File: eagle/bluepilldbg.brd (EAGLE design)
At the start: 39.4 x 19 mm, 9 parts

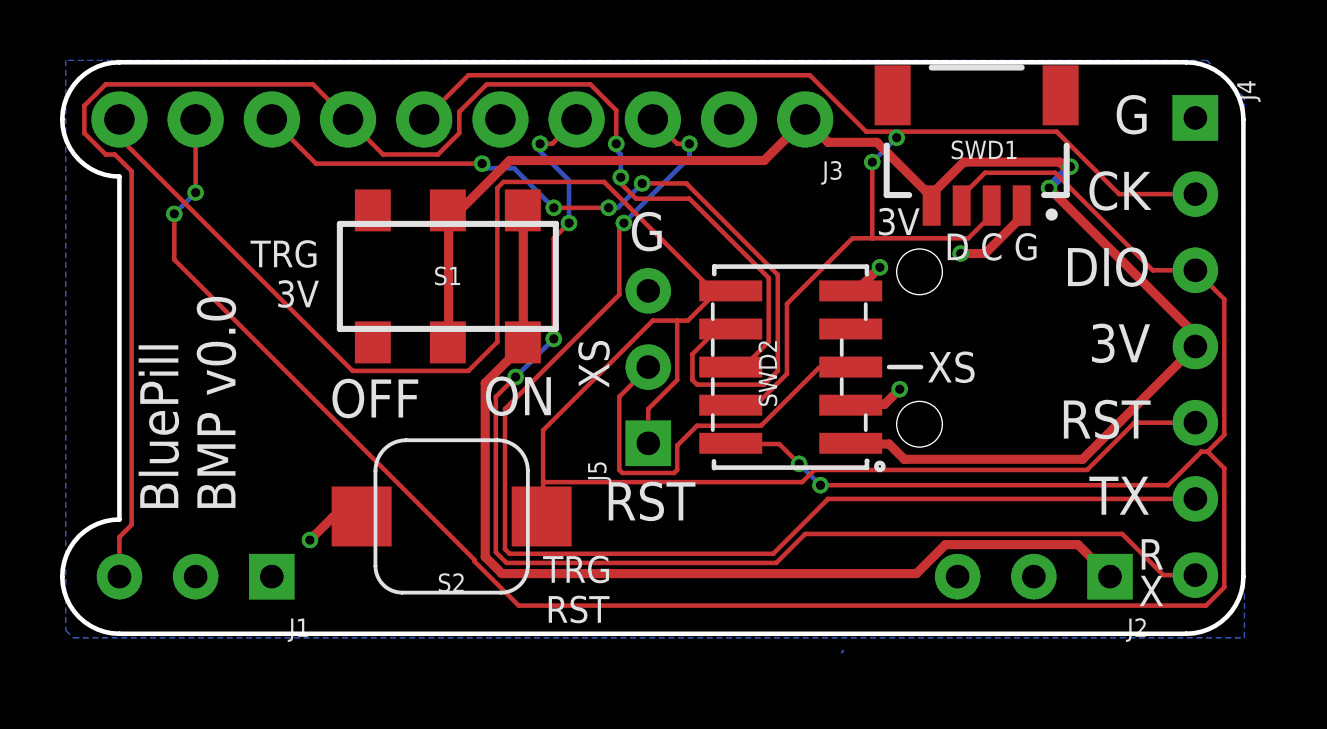
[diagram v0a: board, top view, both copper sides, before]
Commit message: smaller pcb
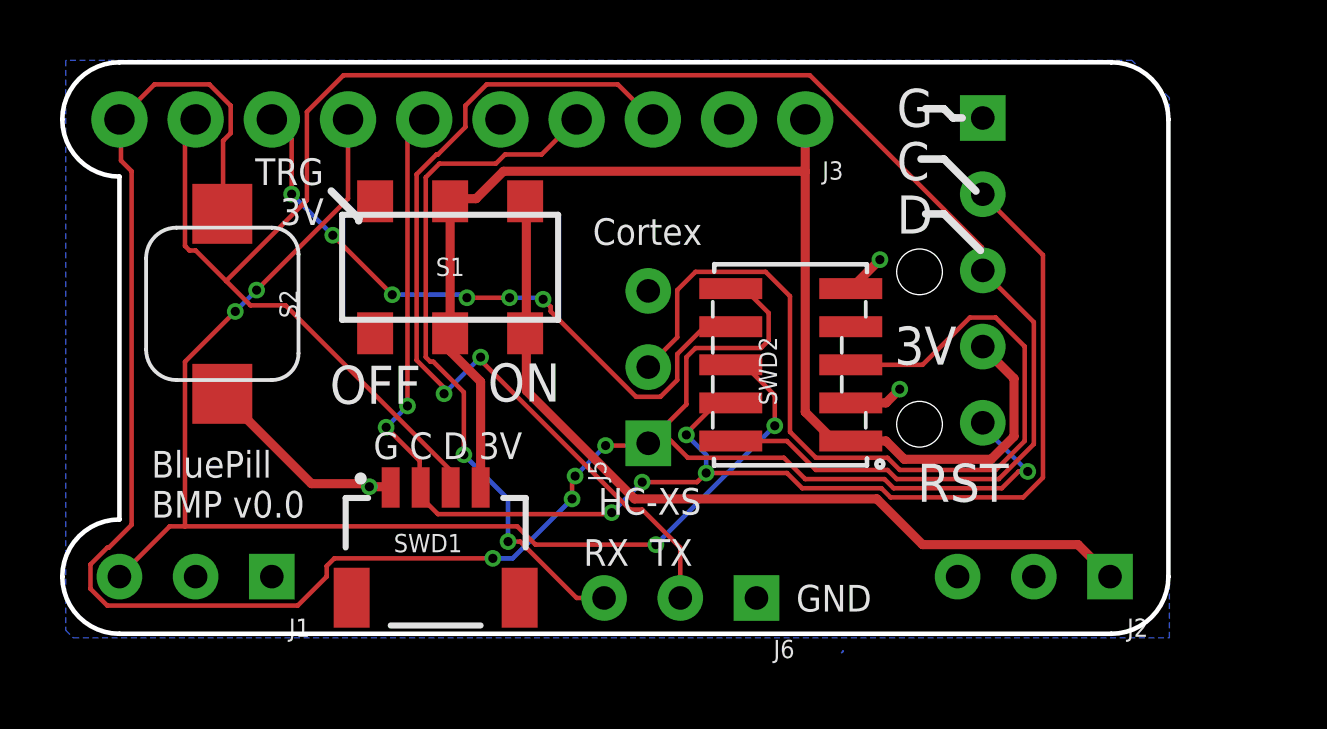
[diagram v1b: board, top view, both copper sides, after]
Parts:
- added J6: (no value), pcnt:1X03_NO_SILK
- J4: device SparkFun-Connectors:1X07_NO_SILK -> pcnt:1X05_SMALLHOLE
- moved SWD1 20.3 mm to (13.1, 5.51), turned to 0 degrees
- moved S2 10.4 mm to (5.97, 11.6), turned to 270 degrees
- moved J4 7.09 mm to (31.3, 17.8)
- moved S1 0.31 mm to (13.6, 12.9)
- moved SWD2 0.08 mm to (24.9, 9.60)
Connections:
- net GND: now also J6.1
- net RX: now also J6.3; no longer J4.7
- net TX: now also J6.2; no longer J4.6
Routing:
- net RX: track 41.0 -> 23.1 mm, vias 4 -> 2
- net HACK_RST: track 13.5 -> 30.6 mm
- net SWDIO: track 83.2 -> 67.4 mm, vias 4 -> 0
- net TX: track 41.4 -> 30.5 mm
- net VREF: track 50.3 -> 43.3 mm, vias 2 -> 0
- net TDO: track 49.9 -> 43.2 mm, vias 2 -> 4
- net TDI: track 28.5 -> 21.8 mm, vias 4 -> 6
- net VCC: track 34.0 -> 28.4 mm
- net SWCLK: track 44.8 -> 49.5 mm, vias 2 -> 6
- net GND: track 8.13 -> 10.1 mm, vias 4 -> 3
- net RST: track 69.5 -> 71.2 mm, vias 0 -> 5
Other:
- board size 39.4 x 19 mm -> 36.9 x 19 mm
- board text added: "Cortex"
- board text added: "G C D"
- board text added: "G C D 3V"
- board text added: "GND"
- board text added: "GND TX RX"
- board text added: "HC-XS"
- board text added: "RX TX"
- board text removed: "D C G"
- board text removed: "G"
- board text removed: "G CK DIO 3V RST TX"
- board text removed: "R X"
- board text removed: "TRG RST"
- board text removed: "XS"

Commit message: Nicer schematics; place part names
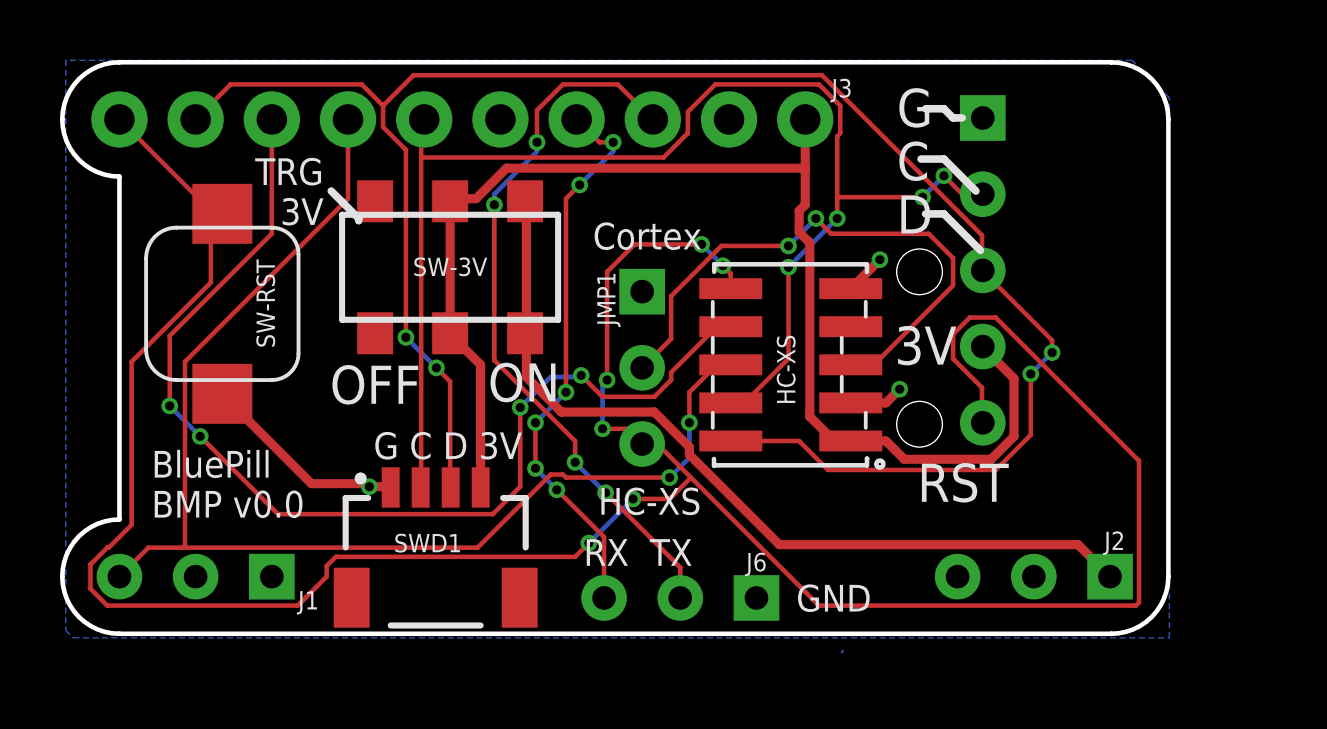
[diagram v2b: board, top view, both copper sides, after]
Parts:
- removed J5: (no value), pcnt:1X03_NO_SILK
- added JMP1: (no value), pcnt:1X03_NO_SILK
- HC-XS: value CORTEX_DEBUG_DBG -> CORTEX_DEBUG
- SWD1: value (none) -> 4P JST-SH
- renumbered S1 to SW-3V, S2 to SW-RST, SWD2 to HC-XS
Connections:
- net GND: now also JMP1.1; no longer J5.3
- net HACK_RST: now also JMP1.2; no longer J5.2
- net RST: now also JMP1.3; no longer J5.1
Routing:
- net RST: track 71.2 -> 89.1 mm, vias 5 -> 6
- net TDI: track 21.8 -> 36.0 mm, vias 6 -> 4
- net HACK_RST: track 30.6 -> 19.2 mm, vias 0 -> 2
- net TX: track 30.5 -> 24.1 mm, vias 2 -> 4
- net SWDIO: track 67.4 -> 62.1 mm, vias 0 -> 4
- net SWCLK: track 49.5 -> 45.1 mm, vias 6 -> 4
- net RX: track 23.1 -> 18.7 mm, vias 2 -> 6
- net TDO: track 43.2 -> 41.2 mm, vias 4 -> 2

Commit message: Re-order JST-SH debug connector to match QWIIC
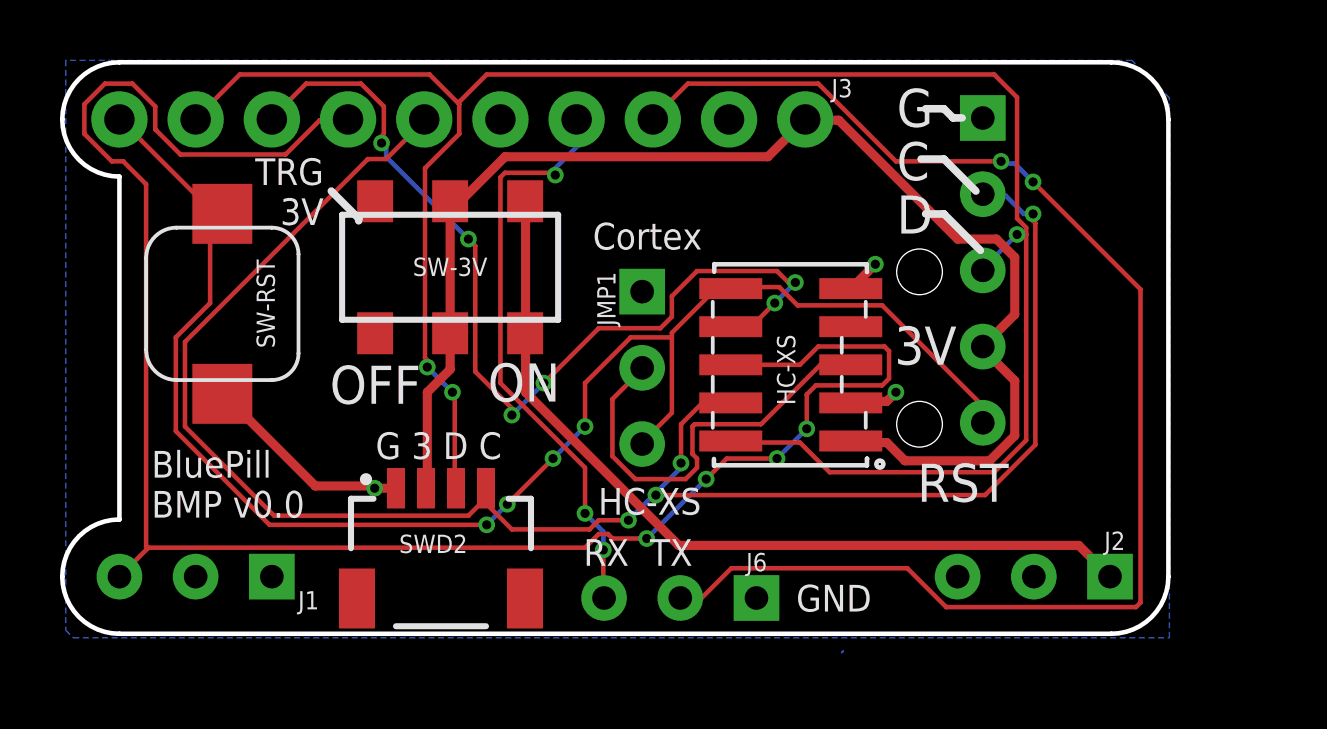
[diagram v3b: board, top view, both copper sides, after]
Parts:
- removed J4: (no value), pcnt:1X05_SMALLHOLE
- added SWD2: 4P JST-SH, pcnt:JST04_1MM_RA
- SWD1: value 4P JST-SH -> (none); device pcnt:JST04_1MM_RA -> pcnt:1X05_SMALLHOLE
- moved SWD1 22.0 mm to (31.3, 17.8), turned to 270 degrees
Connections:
- net GND: now also SWD2.1; no longer J4.1
- net RST: now also SWD1.5; no longer J4.5
- net SWCLK: now also SWD2.4; no longer J4.2
- net SWDIO: now also SWD2.3; no longer J4.3
- net VREF: now also SWD2.2; no longer J4.4
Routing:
- net RST: track 89.1 -> 51.5 mm, vias 6 -> 4
- net TX: track 24.1 -> 46.4 mm, vias 4 -> 2
- net TDO: track 41.2 -> 62.6 mm, vias 2 -> 4
- net SWCLK: track 45.1 -> 60.5 mm
- net SWDIO: track 62.1 -> 67.2 mm, vias 4 -> 3
- net HACK_RST: track 19.2 -> 14.2 mm, vias 2 -> 0
- net TDI: track 36.0 -> 31.5 mm, vias 4 -> 6
- net VREF: track 43.5 -> 44.7 mm
- net RX: track 18.7 -> 19.6 mm, vias 6 -> 3
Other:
- board text added: "G 3 D C"
- board text added: "SWD (not I2C)"
- board text removed: "G C D 3V"

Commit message: add part numbers and BOM
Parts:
- SW-3V: value (none) -> C115375
- SW-RST: value MOMENTARY-SWITCH-SPST-SMD-6.0X3.5MM -> C255816
- SWD1: value (none) -> C124405
- SWD2: value 4P JST-SH -> 4P JST-SH C145956
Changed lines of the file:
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@@
 <attribute name="VALUE" x="26.67" y="19.812" size="0.6096" layer="27" font="vector" ratio="20" rot="R180"/>
 </element>
-<element name="SW-3V" library="pcnt" package="SWITCH_DPDT_SMD_AYZ0202" value="" x="13.5636" y="12.8524" smashed="yes" rot="R180">
+<element name="SW-3V" library="pcnt" package="SWITCH_DPDT_SMD_AYZ0202" value="C115375" x="13.5636" y="12.8524" smashed="yes" rot="R180">
 <attribute name="NAME" x="13.5636" y="12.5624" size="0.6096" layer="25" font="vector" ratio="20" align="bottom-center"/>
 <attribute name="PROD_ID" value="SWCH-08179" x="13.5636" y="12.8524" size="1.778" layer="27" rot="R180" display="off"/>
 <attribute name="SF_ID" value="COM-00597" x="13.5636" y="12.8524" size="1.778" layer="27" rot="R180" display="off"/>
 </element>
-<element name="SW-RST" library="mb-arcade-shield" package="TACTILE_SWITCH_SMD_6.0X3.5MM" value="MOMENTARY-SWITCH-SPST-SMD-6.0X3.5MM" x="5.969" y="11.6332" smashed="yes" rot="R270">
+<element name="SW-RST" library="mb-arcade-shield" package="TACTILE_SWITCH_SMD_6.0X3.5MM" value="C255816" x="5.969" y="11.6332" smashed="yes" rot="R270">
 <attribute name="NAME" x="7.112" y="11.6332" size="0.6096" layer="25" font="vector" ratio="20" rot="R270" align="bottom-center"/>
 <attribute name="PROD_ID" value="SWCH-00815" x="5.969" y="17.1196" size="1.778" layer="27" rot="R270" display="off"/>
@@
 <attribute name="VALUE" x="25.0444" y="3.8608" size="0.6096" layer="27" font="vector" ratio="20" rot="R180"/>
 </element>
-<element name="SWD1" library="pcnt" package="1X05_SMALLHOLE" value="" x="31.3182" y="17.8282" smashed="yes" rot="R270"/>
+<element name="SWD1" library="pcnt" package="1X05_SMALLHOLE" value="C124405" x="31.3182" y="17.8282" smashed="yes" rot="R270"/>
 <element name="JMP1" library="pcnt" package="1X03_NO_SILK" value="" x="19.9644" y="12.0396" smashed="yes" rot="R270">
 <attribute name="NAME" x="18.4658" y="12.7" size="0.6096" layer="25" font="vector" ratio="20" rot="R270"/>
 <attribute name="VALUE" x="17.9324" y="13.3096" size="0.6096" layer="27" font="vector" ratio="20" rot="R270"/>
 </element>
-<element name="SWD2" library="pcnt" package="JST04_1MM_RA" value="4P JST-SH" x="13.2588" y="5.4864" smashed="yes">
+<element name="SWD2" library="pcnt" package="JST04_1MM_RA" value="4P JST-SH C145956" x="13.2588" y="5.4864" smashed="yes">
 <attribute name="NAME" x="11.8618" y="3.3274" size="0.6096" layer="25" font="vector" ratio="20"/>
 <attribute name="PROD_ID" value="CONN-10310" x="13.2588" y="5.4864" size="1.778" layer="27" display="off"/>
